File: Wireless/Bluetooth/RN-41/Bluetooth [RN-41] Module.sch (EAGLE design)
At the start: 12 parts

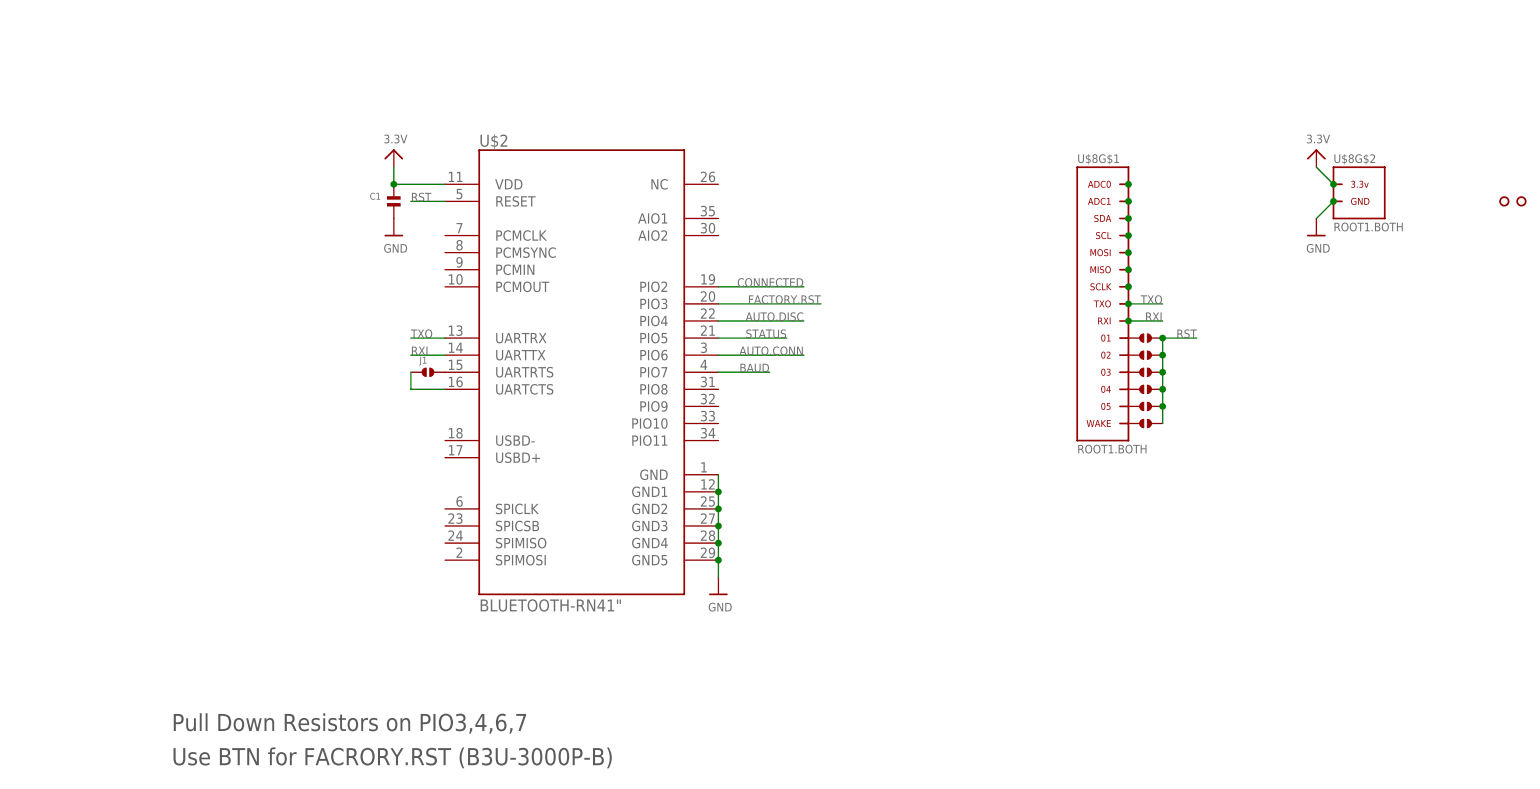
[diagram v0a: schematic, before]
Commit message: Completed Bluetooth (RN-41) Module
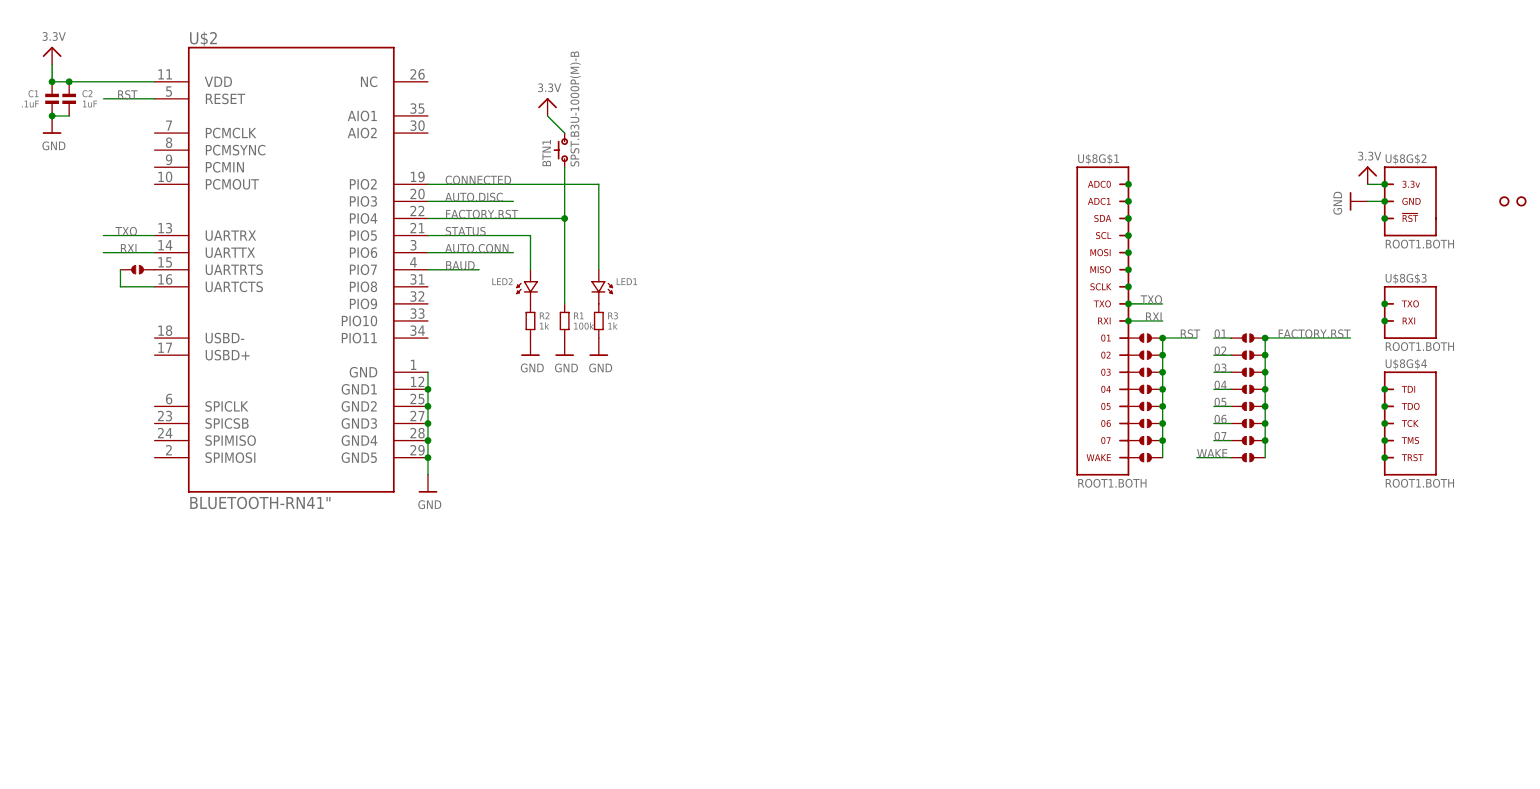
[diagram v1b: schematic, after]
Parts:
- removed 03: (no value), .solderjumper:SOLDERJUMPER.2.SML
- added 08, J10, J11, J12, J13, J14, J15, J2, J4, J8, J9: (no value), .solderjumper:SOLDERJUMPER.2.SML
- added BTN1: SPST.B3U-1000P(M)-B, omron:SPST.B3U-1000P(M)-B
- added C2: 1uF, .standardparts:CAPACITOR.0603
- added LED1, LED2: (no value), .standardparts:LED.0603
- added R1: 100k, .standardparts:RESISTOR.0603
- added R2, R3: 1k, .standardparts:RESISTOR.0603
- C1: value (none) -> .1uF
- renumbered 02 to J3
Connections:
- new net 01: J2.1, J4.1, U$8G$1.01
- new net 02: J10.1, J3.1, U$8G$1.02
- new net 03: J11.1, J5.1, U$8G$1.03
- new net 04: J12.1, J6.1, U$8G$1.04
- new net 05: J13.1, J7.1, U$8G$1.05
- new net 06: J14.1, J8.1, U$8G$1.06
- new net 07: J15.1, J9.1, U$8G$1.07
- new net N$16: U$8G$3.RXI
- new net N$17: U$8G$3.TXO
- new net N$19: U$8G$2.!RST
- new net N$23: LED1.2, R3.1
- new net WAKE: 01.1, 08.1, U$8G$1.WAKE
- net 3.3V: now also BTN1.2, C2.1
- net AUTO.DISC: now also U$2.PIO3; no longer U$2.PIO4
- net CONNECTED: now also LED1.1
- net FACTORY.RST: now also 01.2, BTN1.1, J10.2, J11.2, J12.2, J13.2, J14.2, J15.2, J4.2, R1.1, U$2.PIO4; no longer U$2.PIO3
- net GND: now also C2.2, R1.2, R2.2, R3.2
- net N$10: now also LED2.2, R2.1; no longer 01.1, U$8G$1.01
- net N$11: now also U$8G$4.TRST; no longer J3.1, U$8G$1.02
- net N$12: now also U$8G$4.TMS; no longer 03.1, U$8G$1.03
- net N$13: now also U$8G$4.TCK; no longer J5.1, U$8G$1.04
- net N$14: now also U$8G$4.TDO; no longer J6.1, U$8G$1.05
- net N$15: now also U$8G$4.TDI; no longer J7.1, U$8G$1.WAKE
- net RST: now also 08.2, J2.2, J8.2, J9.2; no longer 01.2, 03.2
- net STATUS: now also LED2.1
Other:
- note removed: "Pull Down Resistors on PIO3,4,6,7"
- note removed: "Use BTN for FACRORY.RST (B3U-3000P-B)"
- moved on the sheet: C1, U$2
